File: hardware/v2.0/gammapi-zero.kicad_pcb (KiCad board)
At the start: 4 copper layers, 65 x 30 mm, 209 parts, among them IC1 IS42S16160J-6BLI, IC3 LM4040AIM3-2.0_NOPB, IC4 LTC2622IMS8#PBF, IC5 LTC6409IUDB#TRPBF, IC6 ADS6122IRHBT, J1 Conn_02x20_Counter_Clockwise, J2 GPDI_C_1.3, J3 USB_C_Receptacle_USB2.0_14P, J4 USB_C_Receptacle_USB2.0_14P, J5 USB_C_Receptacle_USB2.0_14P, J6 Micro_SD_Card_Det2, J7 RSP-122811-01, J8 BM04B-ACHSS-A-GAN-TF_LF__SN_, SW1 SW_Push, SW2 SW_Push, U1 ECP5U-25F-CABGA256, U10 TPD2EUSB30A, U12 W25Q128JVS, U2 LTC3407AEDD-2_PBF, U3 TLV62569DBV, U5 TCR5FM18A, U6 PCA9306DC1, U7 TPD2EUSB30A, U8 TPD2EUSB30A, U9 FT231XQ, Y1 SG-8018CG 50.000000MHz, Y2 SG-8018CG 50.000000MHz

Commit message: Layout fixes
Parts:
- U10, U7, U8: footprint Package_TO_SOT_SMD:Texas_DRT-3 -> Library:Texas_DRT-3
- moved C3 0.96 mm to (153.7, 104.3), turned to -90 degrees
- moved C16 0.91 mm to (151.8, 106.5)
- moved C7 0.61 mm to (151.8, 104.9), turned to 180 degrees
- moved REF** 0.46 mm to (128.1, 111.2)
- moved R1 0.31 mm to (160.9, 112.0)
- moved C28 0.24 mm to (152.1, 107.9)
- moved TP3 0.19 mm to (117.9, 106.5)
- moved REF** 0.16 mm to (120.3, 110.6)
- moved C10 0.13 mm to (148.9, 105.0)
- moved C2 0.13 mm to (149.8, 108.1)
- moved C63 0.07 mm to (167.3, 110.1)
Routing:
- net +1V1: track 61.1 -> 59.4 mm, vias 8 -> 5
- net GND: track 99.3 -> 98.8 mm, vias 108 -> 102

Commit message: Layout fixes
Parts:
- moved R47 0.07 mm to (139.9, 106.9)
- moved C83 0.07 mm to (172.5, 102.3)
- moved IC3 0.07 mm to (175.0, 102.5)

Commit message: Layout adjustments
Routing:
- net +3V3: track 144.3 -> 143.7 mm
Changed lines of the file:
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@@
 	)
 	(segment
-		(start 144.97153 108.71153)
-		(end 145.351296 108.71153)
+		(start 144.400001 107.760001)
+		(end 145.351296 108.711296)
 		(width 0.2)
 		(layer "In2.Cu")
@@
 	)
 	(segment
-		(start 146.125 117.65)
-		(end 146.044024 117.65)
+		(start 149.775 115.782247)
+		(end 148.891247 116.666)
 		(width 0.2)
 		(layer "In2.Cu")
@@
 	)
 	(segment
-		(start 137.204322 118.909)
-		(end 136.46591 118.909)
+		(start 137.402589 118.907411)
+		(end 137.205911 118.907411)
 		(width 0.2)
 		(layer "In2.Cu")
@@
 	)
 	(segment
-		(start 144.400001 107.209964)
-		(end 144.400001 108.140001)
+		(start 145.351296 108.71153)
+		(end 145.380765 108.741)
 		(width 0.2)
 		(layer "In2.Cu")
@@
 	)
 	(segment
-		(start 141.316 116.941)
-		(end 138.435667 116.941)
+		(start 148.618024 109.059)
+		(end 148.891 109.331976)
 		(width 0.2)
 		(layer "In2.Cu")
@@
 	)
 	(segment
-		(start 145.367171 117.65)
-		(end 142.025 117.65)
+		(start 145.351296 108.711296)
+		(end 145.351296 108.71153)
 		(width 0.2)
 		(layer "In2.Cu")
@@
 	)
 	(segment
-		(start 145.351296 108.71153)
-		(end 145.380765 108.741)
+		(start 146.044024 117.65)
+		(end 146.043024 117.651)
 		(width 0.2)
 		(layer "In2.Cu")
@@
 	)
 	(segment
-		(start 147.109 116.666)
-		(end 146.125 117.65)
+		(start 138.435667 116.941)
+		(end 137.61 117.766667)
 		(width 0.2)
 		(layer "In2.Cu")
@@
 	)
 	(segment
-		(start 144.399147 107.20911)
-		(end 144.400001 107.209964)
+		(start 141.316 116.941)
+		(end 138.435667 116.941)
 		(width 0.2)
 		(layer "In2.Cu")
@@
 	)
 	(segment
-		(start 136.46591 118.909)
-		(end 136.149 119.22591)
+		(start 137.204322 118.909)
+		(end 136.46591 118.909)
 		(width 0.2)
 		(layer "In2.Cu")
@@
 	)
 	(segment
-		(start 146.044024 117.65)
-		(end 146.043024 117.651)
+		(start 137.61 118.7)
+		(end 137.402589 118.907411)
+		(width 0.2)
+		(layer "In2.Cu")
+		(net 2)
+	)
+	(segment
+		(start 148.891 109.341)
+		(end 149.775 110.225)
 		(width 0.2)
 		(layer "In2.Cu")
@@
 	)
 	(segment
-		(start 145.380765 108.741)
-		(end 148.291 108.741)
+		(start 136.149 119.22591)
+		(end 136.149 119.227667)
 		(width 0.2)
 		(layer "In2.Cu")
@@
 	)
 	(segment
-		(start 148.618024 109.059)
-		(end 148.891 109.331976)
+		(start 146.125 117.65)
+		(end 146.044024 117.65)
 		(width 0.2)
 		(layer "In2.Cu")
@@
 	)
 	(segment
-		(start 149.775 110.225)
-		(end 149.775 115.782247)
-		(width 0.2)
-		(layer "In2.Cu")
-		(net 2)
-	)
-	(segment
-		(start 148.891 109.331976)
-		(end 148.891 109.341)
+		(start 148.891247 116.666)
+		(end 147.109 116.666)
 		(width 0.2)
 		(layer "In2.Cu")
@@
 	)
 	(segment
-		(start 149.775 115.782247)
-		(end 148.891247 116.666)
+		(start 137.61 117.766667)
+		(end 137.61 118.7)
 		(width 0.2)
 		(layer "In2.Cu")
@@
 	)
 	(segment
-		(start 137.61 118.7)
-		(end 137.402589 118.907411)
+		(start 137.205911 118.907411)
+		(end 137.204322 118.909)
 		(width 0.2)
 		(layer "In2.Cu")
@@
 	)
 	(segment
-		(start 148.891 109.341)
-		(end 149.775 110.225)
+		(start 148.291 108.741)
+		(end 148.609 109.059)
 		(width 0.2)
 		(layer "In2.Cu")
@@
 	)
 	(segment
-		(start 148.291 108.741)
-		(end 148.609 109.059)
+		(start 147.109 116.666)
+		(end 146.125 117.65)
 		(width 0.2)
 		(layer "In2.Cu")
@@
 	)
 	(segment
-		(start 138.435667 116.941)
-		(end 137.61 117.766667)
+		(start 136.149 119.227667)
+		(end 135.950381 119.426286)
 		(width 0.2)
 		(layer "In2.Cu")
@@
 	)
 	(segment
-		(start 144.400001 108.140001)
-		(end 144.97153 108.71153)
+		(start 145.380765 108.741)
+		(end 148.291 108.741)
 		(width 0.2)
 		(layer "In2.Cu")
@@
 	)
 	(segment
-		(start 137.402589 118.907411)
-		(end 137.205911 118.907411)
+		(start 148.891 109.331976)
+		(end 148.891 109.341)
 		(width 0.2)
 		(layer "In2.Cu")
@@
 	)
 	(segment
-		(start 137.61 117.766667)
-		(end 137.61 118.7)
+		(start 142.025 117.65)
+		(end 141.316 116.941)
 		(width 0.2)
 		(layer "In2.Cu")
@@
 	)
 	(segment
-		(start 136.149 119.22591)
-		(end 136.149 119.227667)
+		(start 136.46591 118.909)
+		(end 136.149 119.22591)
 		(width 0.2)
 		(layer "In2.Cu")
@@
 	)
 	(segment
-		(start 136.149 119.227667)
-		(end 135.950381 119.426286)
+		(start 149.775 110.225)
+		(end 149.775 115.782247)
 		(width 0.2)
 		(layer "In2.Cu")
@@
 	)
 	(segment
-		(start 148.891247 116.666)
-		(end 147.109 116.666)
+		(start 144.399147 107.20911)
+		(end 144.400001 107.209964)
 		(width 0.2)
 		(layer "In2.Cu")
@@
 	)
 	(segment
-		(start 142.025 117.65)
-		(end 141.316 116.941)
+		(start 145.367171 117.65)
+		(end 142.025 117.65)
 		(width 0.2)
 		(layer "In2.Cu")
@@
 	)
 	(segment
-		(start 137.205911 118.907411)
-		(end 137.204322 118.909)
+		(start 144.400001 107.209964)
+		(end 144.400001 107.760001)
 		(width 0.2)
 		(layer "In2.Cu")
@@
 	)
 	(segment
-		(start 147.15399 112)
-		(end 147.025 112)
-		(width 0.2)
-		(layer "In2.Cu")
-		(net 18)
-	)
-	(segment
 		(start 147.303631 102.715329)
 		(end 148.792358 102.715329)
@@
 	)
 	(segment
-		(start 147.025 112)
-		(end 146.675 111.65)
-		(width 0.2)
-		(layer "In2.Cu")
-		(net 18)
-	)
-	(segment
 		(start 148.792358 102.715329)
 		(end 149.213999 103.13697)
@@
 	)
 	(segment
+		(start 146.23 104.52)
+		(end 146.56 104.19)
+		(width 0.3)
+		(layer "In2.Cu")
+		(net 54)
+	)
+	(segment
 		(start 128.243999 103.32)
 		(end 128.237999 103.326)
@@
 	)
 	(segment
-		(start 141.685 108.24214)
-		(end 142.04214 108.24214)
-		(width 0.15)
-		(layer "In2.Cu")
-		(net 88)
-	)
-	(segment
-		(start 142.857 109.057)
-		(end 144.825596 109.057)
-		(width 0.15)
-		(layer "In2.Cu")
-		(net 88)
-	)
-	(segment
-		(start 147.107 109.057)
-		(end 147.571233 109.521233)
+		(start 142.04214 108.24214)
+		(end 142.82753 109.02753)
 		(width 0.15)
 		(layer "In2.Cu")
@@
 	)
 	(segment
-		(start 142.04214 108.24214)
-		(end 142.857 109.057)
+		(start 145.249874 109.057)
+		(end 147.107 109.057)
 		(width 0.15)
 		(layer "In2.Cu")
@@
 	)
 	(segment
-		(start 145.249874 109.057)
-		(end 147.107 109.057)
+		(start 141.685 108.24214)
+		(end 142.04214 108.24214)
 		(width 0.15)
 		(layer "In2.Cu")
@@
 	)
 	(segment
-		(start 144.825596 109.057)
-		(end 144.855066 109.02753)
+		(start 147.107 109.057)
+		(end 147.571233 109.521233)
 		(width 0.15)
 		(layer "In2.Cu")
@@
 	)
 	(segment
-		(start 144.855066 109.02753)
+		(start 142.82753 109.02753)
 		(end 145.220404 109.02753)
 		(width 0.15)
@@
 	)
 	(segment
-		(start 161.9 105.36)
-		(end 161.9 105.448617)
+		(start 158.28 107.65)
+		(end 156.870868 107.65)
 		(width 0.15)
 		(layer "In2.Cu")
@@
 	)
 	(segment
-		(start 156.510869 108.010001)
-		(end 156.510868 108.01)
+		(start 161.078617 106.27)
+		(end 159.66 106.27)
 		(width 0.15)
 		(layer "In2.Cu")
@@
 	)
 	(segment
-		(start 161.228617 106.12)
-		(end 159.9 106.12)
+		(start 161.9 105.448617)
+		(end 161.078617 106.27)
 		(width 0.15)
 		(layer "In2.Cu")
@@
 	)
 	(segment
-		(start 156.872255 108.010001)
-		(end 156.510869 108.010001)
+		(start 161.9 105.36)
+		(end 161.9 105.448617)
 		(width 0.15)
 		(layer "In2.Cu")
@@
 	)
 	(segment
-		(start 161.9 105.448617)
-		(end 161.228617 106.12)
+		(start 156.510869 108.010001)
+		(end 156.510868 108.01)
 		(width 0.15)
 		(layer "In2.Cu")
@@
 	)
 	(segment
-		(start 158.17 107.85)
-		(end 157.032256 107.85)
+		(start 159.66 106.27)
+		(end 158.28 107.65)
 		(width 0.15)
 		(layer "In2.Cu")
@@
 	)
 	(segment
-		(start 159.9 106.12)
-		(end 158.17 107.85)
+		(start 156.870868 107.65)
+		(end 156.510869 108.009999)
 		(width 0.15)
 		(layer "In2.Cu")
@@
 	)
 	(segment
-		(start 157.032256 107.85)
-		(end 156.872255 108.010001)
+		(start 156.510869 108.009999)
+		(end 156.510869 108.010001)
 		(width 0.15)
 		(layer "In2.Cu")
@@
 		(polygon
 			(pts
-				(xy 149 112) (xy 149 120) (xy 115.65 120) (xy 115.66 112)
+				(xy 146.16 112.01) (xy 146.87 112.57) (xy 146.87 120.01) (xy 115.65 120) (xy 115.66 112)
 			)
 		)

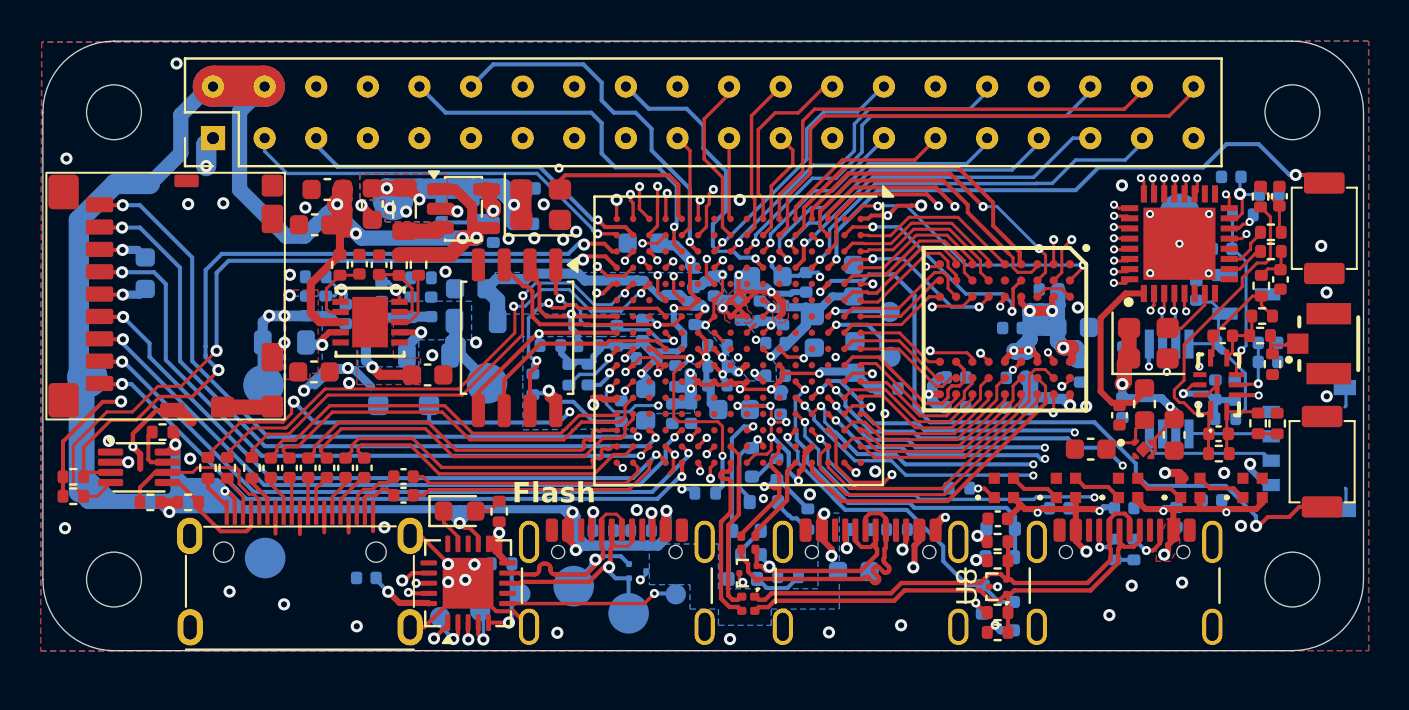
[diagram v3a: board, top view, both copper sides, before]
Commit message: ADC digital line power fix
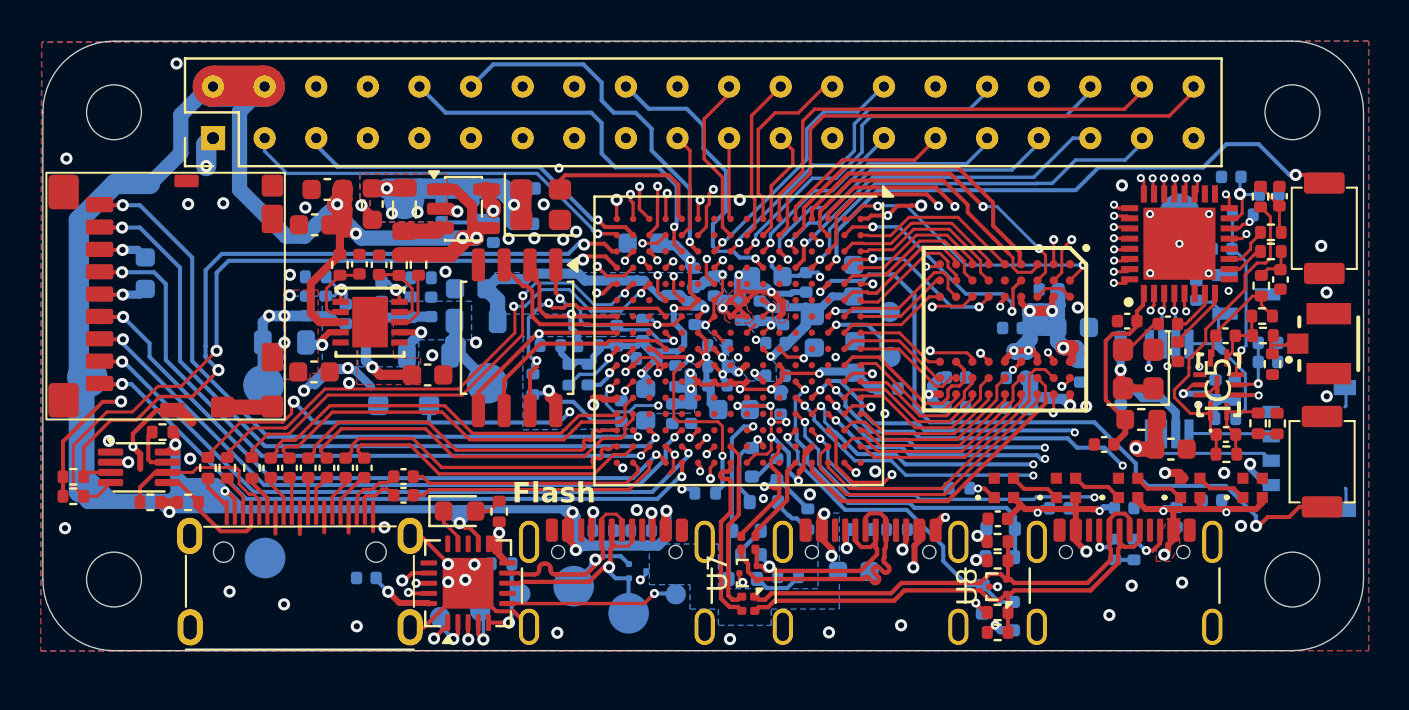
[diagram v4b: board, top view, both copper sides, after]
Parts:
- removed U5: TCR5FM18A, TCR5FM50A:TCR5FM50A
- added C61: 100n, Capacitor_SMD:C_0402_1005Metric, F.Cu at (171.6, 105.3)
- added C64: 100n, Capacitor_SMD:C_0402_1005Metric, F.Cu at (169.1, 103.8)
- C63: value 10u -> 100n; footprint Capacitor_SMD:C_0603_1608Metric -> Capacitor_SMD:C_0402_1005Metric
- U10, U7, U8: footprint Library:Texas_DRT-3 -> Package_TO_SOT_SMD:Texas_DRT-3
- moved C63 7.24 mm to (171.1, 103.9), turned to 0 degrees
- moved C65 1.63 mm to (168.0, 109.8), turned to 180 degrees
- moved Y2 1.36 mm to (169.7, 106.1), turned to 90 degrees
- moved FB2 0.78 mm to (169.8, 108.6), turned to 180 degrees
- moved C62 0.72 mm to (171.3, 110.1), turned to 0 degrees
- moved C82 0.64 mm to (168.8, 107.4)
- moved TP4 0.55 mm to (133.5, 97.8)
- moved C55 0.53 mm to (168.8, 105.0)
- moved R60 0.37 mm to (174.0, 110.3)
- moved C78 0.37 mm to (174.0, 109.4)
- moved C84 0.14 mm to (174.0, 104.5)
- moved R57 0.14 mm to (175.8, 104.5)
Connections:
- net FILTERED_1V8 renamed FILTERED_3V3
- C63 pad 1: +1V8 -> /ADC/CLK+
- C63 pad 2: GND -> Net-(IC6-CLKP)
- FB2 pad 1: +1V8 -> +3V3
- IC6 pad 7: /ADC/CLK+ -> Net-(IC6-CLKP)
- IC6 pad 8: GND -> Net-(IC6-CLKM)
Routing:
- net Net-(IC6-CLKM): track 0.00 -> 3.14 mm
- net +1V8: track 2.87 -> 0.00 mm
- net Net-(IC6-CLKP): track 0.00 -> 2.29 mm
- net +3V3: track 143.7 -> 142.5 mm, vias 36 -> 35
- net /ADC/CLK+: track 2.89 -> 2.26 mm
- net /GPIO14: track 19.8 -> 20.4 mm
- net GND: vias 102 -> 103
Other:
- board text added: "GammaPi Zero v2.7"
- board text removed: "GammaPi Zero v2.6"
